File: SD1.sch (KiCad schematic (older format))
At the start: 43 parts, among them J103 JST ZH 1.5mm 1x5, J107 FPC PMS, Q101 BSS138, Q102 PDTC114EU,115, SW103 Multidirection_Switch, SW104 Multifunction_Switch, U101 TLV70233_SOT23-5, U102 ER-TFTM028-4, U104 CC2652P, U106 EKMC1691111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

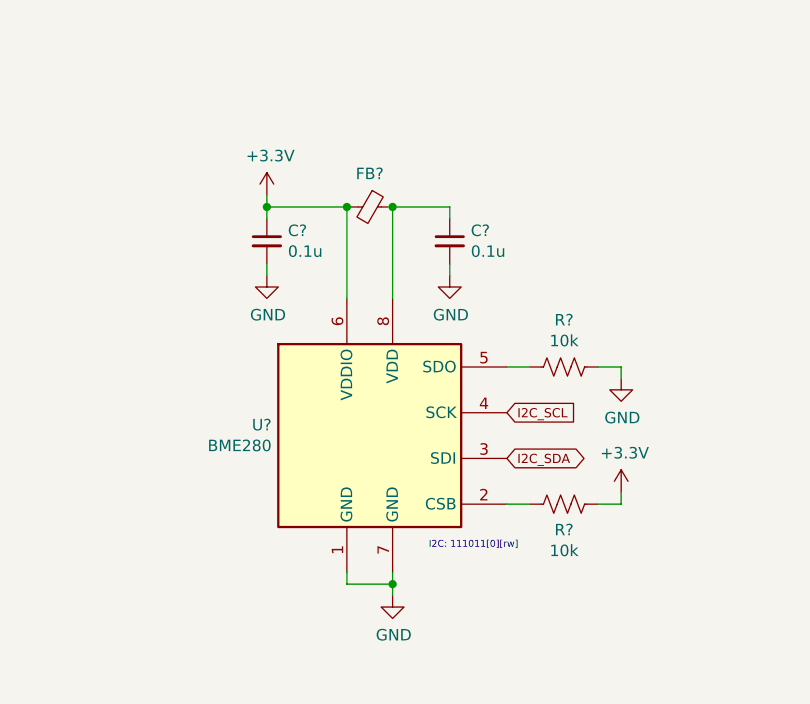
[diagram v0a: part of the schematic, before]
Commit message: Minor part picking and annotation
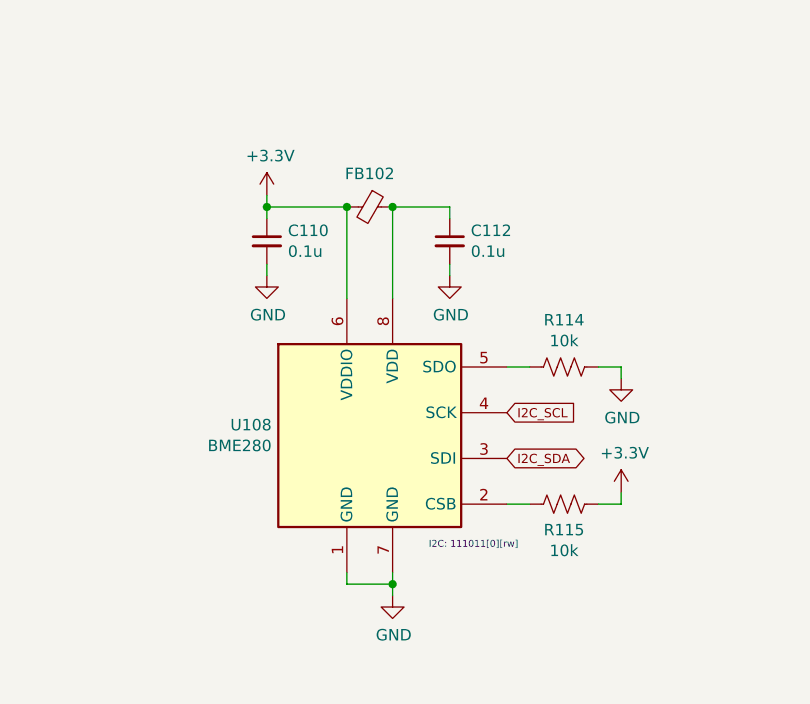
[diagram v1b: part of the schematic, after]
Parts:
- J103: Digikey (none) -> 455-1684-1-ND; LCSC (none) -> C265440; MPN (none) -> B5B-ZR-SM4-TF(LF)(SN)
- SW104: LCSC (none) -> C502286; MPN (none) -> K1-1508SA-03; Note (none) -> SMD Multi-Directional Switch Thumb
- U108: renamed from U?; LCSC C92489 -> C92489; Manufacturer (none) -> Bosch
- gave numbers to parts that had none: 5
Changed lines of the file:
@@
 F 2 "mylib:K1-1508SA-01" H 5200 9460 50  0001 C CNN
 F 3 "~" H 5350 9560 50  0001 C CNN
+F 4 "C502286" H 5350 9300 50  0001 C CNN "LCSC"
+F 5 "K1-1508SA-03" H 5350 9300 50  0001 C CNN "MPN"
+F 6 "SMD Multi-Directional Switch Thumb" H 5350 9300 50  0001 C CNN "Note"
 	1    5350 9300
 	1    0    0    -1
@@
 F 3 "~" H 6250 8100 50  0001 C CNN
 F 4 "1.5mm 01x05 JST ZH" H 6250 8100 50  0001 C CNN "Note"
+F 5 "B5B-ZR-SM4-TF(LF)(SN)" H 6250 8100 50  0001 C CNN "MPN"
+F 6 "455-1684-1-ND" H 6250 8100 50  0001 C CNN "Digikey"
+F 7 "C265440" H 6250 8100 50  0001 C CNN "LCSC"
 	1    6250 8100
 	1    0    0    1
@@
 SERCOM 0
 $Comp
-L power:GND #PWR?
+L power:GND #PWR0187
 U 1 1 5FB0CAA2
 P 12050 8800
-F 0 "#PWR?" H 12050 8550 50  0001 C CNN
+F 0 "#PWR0187" H 12050 8550 50  0001 C CNN
 F 1 "GND" H 12055 8627 50  0000 C CNN
 F 2 "" H 12050 8800 50  0001 C CNN
@@
 	11500 7150 11500 7100
 $Comp
-L power:+3.3V #PWR?
+L power:+3.3V #PWR0188
 U 1 1 5FB0CAA9
 P 11500 7050
-F 0 "#PWR?" H 11500 6900 50  0001 C CNN
+F 0 "#PWR0188" H 11500 6900 50  0001 C CNN
 F 1 "+3.3V" H 11515 7223 50  0000 C CNN
 F 2 "" H 11500 7050 50  0001 C CNN
@@
 $EndComp
 $Comp
-L Sensor:BME280 U?
+L Sensor:BME280 U108
 U 1 1 5FB0CAB4
 P 11950 8100
-F 0 "U?" H 11521 8146 50  0000 R CNN
+F 0 "U108" H 11521 8146 50  0000 R CNN
 F 1 "BME280" H 11521 8055 50  0000 R CNN
 F 2 "Package_LGA:Bosch_LGA-8_2.5x2.5mm_P0.65mm_ClockwisePinNumbering" H 13450 7650 50  0001 C CNN
@@
 F 6 "Humidity Temperature Sensor 0 ~ 100% RH I²C, SPI ±3% 1s Surface Mount" H 11950 8100 50  0001 C CNN "Note"
 F 7 "262-BME280" H 11950 8100 50  0001 C CNN "Mouser"
-F 8 " C92489 " H 11950 8100 50  0001 C CNN "LCSC"
+F 8 "C92489 " H 11950 8100 50  0001 C CNN "LCSC"
+F 9 "Bosch" H 11950 8100 50  0001 C CNN "Manufacturer"
 	1    11950 8100
 	1    0    0    -1
@@
 	12550 8400 12650 8400
 $Comp
-L power:+3.3V #PWR?
+L power:+3.3V #PWR0189
 U 1 1 5FB0CABB
 P 13050 8350
-F 0 "#PWR?" H 13050 8200 50  0001 C CNN
+F 0 "#PWR0189" H 13050 8200 50  0001 C CNN
 F 1 "+3.3V" H 13065 8523 50  0000 C CNN
 F 2 "" H 13050 8350 50  0001 C CNN
@@
 	13050 8400 13050 8350
 $Comp
-L Device:R_US R?
+L Device:R_US R114
 U 1 1 5FB0CAC7
 P 12800 7800
-F 0 "R?" V 13005 7800 50  0000 C CNN
+F 0 "R114" V 13005 7800 50  0000 C CNN
 F 1 "10k" V 12914 7800 50  0000 C CNN
 F 2 "Resistor_SMD:R_0603_1608Metric" H 12800 7800 60  0001 C CNN
@@
 $EndComp
 $Comp
-L Device:R_US R?
+L Device:R_US R115
 U 1 1 5FB0CAD0
 P 12800 8400
-F 0 "R?" V 12687 8400 50  0000 C CNN
+F 0 "R115" V 12687 8400 50  0000 C CNN
 F 1 "10k" V 12596 8400 50  0000 C CNN
 F 2 "Resistor_SMD:R_0603_1608Metric" H 12800 8400 60  0001 C CNN
@@
 $EndComp
 $Comp
-L Device:Ferrite_Bead_Small FB?
+L Device:Ferrite_Bead_Small FB102
 U 1 1 5FB0CADA
 P 11950 7100
-F 0 "FB?" V 11805 7100 50  0000 C CNN
+F 0 "FB102" V 11805 7100 50  0000 C CNN
 F 1 "Ferrite_Bead_Small" V 11804 7100 50  0001 C CNN
 F 2 "Inductor_SMD:L_0603_1608Metric" V 11880 7100 50  0001 C CNN
@@
 Connection ~ 11500 7100
 $Comp
-L power:GND #PWR?
+L power:GND #PWR0190
 U 1 1 5FB0CAE3
 P 12300 7400
-F 0 "#PWR?" H 12300 7150 50  0001 C CNN
+F 0 "#PWR0190" H 12300 7150 50  0001 C CNN
 F 1 "GND" H 12305 7227 50  0000 C CNN
 F 2 "" H 12300 7400 50  0001 C CNN
@@
 	12300 7350 12300 7400
 $Comp
-L power:GND #PWR?
+L power:GND #PWR0191
 U 1 1 5FB0CAED
 P 11500 7400
-F 0 "#PWR?" H 11500 7150 50  0001 C CNN
+F 0 "#PWR0191" H 11500 7150 50  0001 C CNN
 F 1 "GND" H 11505 7227 50  0000 C CNN
 F 2 "" H 11500 7400 50  0001 C CNN
@@
 P 11500 7250
 AR Path="/5E360A9B/5FB0CAFA" Ref="C?"  Part="1"
-AR Path="/5FB0CAFA" Ref="C?"  Part="1"
+AR Path="/5FB0CAFA" Ref="C110"  Part="1"
 AR Path="/5E49A000/5FB0CAFA" Ref="C?"  Part="1"
 AR Path="/5E5C8043/5E49A000/5FB0CAFA" Ref="C?"  Part="1"
 AR Path="/5E5C8043/5EAB3002/5FB0CAFA" Ref="C?"  Part="1"
 AR Path="/5E5C8043/5FB0CAFA" Ref="C?"  Part="1"
-F 0 "C?" H 11592 7296 50  0000 L CNN
+F 0 "C110" H 11592 7296 50  0000 L CNN
 F 1 "0.1u" H 11592 7205 50  0000 L CNN
 F 2 "Capacitor_SMD:C_0603_1608Metric" H 11500 7250 50  0001 C CNN
@@
 P 12300 7250
 AR Path="/5E360A9B/5FB0CB03" Ref="C?"  Part="1"
-AR Path="/5FB0CB03" Ref="C?"  Part="1"
+AR Path="/5FB0CB03" Ref="C112"  Part="1"
 AR Path="/5E49A000/5FB0CB03" Ref="C?"  Part="1"
 AR Path="/5E5C8043/5E49A000/5FB0CB03" Ref="C?"  Part="1"
 AR Path="/5E5C8043/5EAB3002/5FB0CB03" Ref="C?"  Part="1"
 AR Path="/5E5C8043/5FB0CB03" Ref="C?"  Part="1"
-F 0 "C?" H 12392 7296 50  0000 L CNN
+F 0 "C112" H 12392 7296 50  0000 L CNN
 F 1 "0.1u" H 12392 7205 50  0000 L CNN
 F 2 "Capacitor_SMD:C_0603_1608Metric" H 12300 7250 50  0001 C CNN
@@
 	12550 7800 12650 7800
 $Comp
-L power:GND #PWR?
+L power:GND #PWR0192
 U 1 1 5FB0CB0B
 P 13050 7850
-F 0 "#PWR?" H 13050 7600 50  0001 C CNN
+F 0 "#PWR0192" H 13050 7600 50  0001 C CNN
 F 1 "GND" H 13055 7677 50  0000 C CNN
 F 2 "" H 13050 7850 50  0001 C CNN

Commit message: Add SCD30 co2 sensor
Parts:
- added C114: 10u, Capacitor_SMD:C_0603_1608Metric, symbol Device:C_Small
- added U109: SCD30, mylib:SCD30, symbol mylib:SCD30
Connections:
- wire segments 189 -> 199
- no-connect marks 29 -> 31
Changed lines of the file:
@@
 Text Notes 12600 8600 2    30   ~ 0
 I2C: 111011[0][rw]
+Text Notes -35300 -1500 1    50   ~ 0
+SERCOM 0
+Text Notes -35300 -1500 1    50   ~ 0
+SERCOM 0
+Text Notes -35300 -1500 1    50   ~ 0
+SERCOM 0
+Text Notes -35300 -1500 1    50   ~ 0
+SERCOM 0
+Text Notes -35300 -1500 1    50   ~ 0
+SERCOM 0
+Text Notes -35300 -1500 1    50   ~ 0
+SERCOM 0
+Text Notes -35300 -1500 1    50   ~ 0
+SERCOM 0
+Text Notes -35300 -1500 1    50   ~ 0
+SERCOM 0
+Text Notes -35300 -1500 1    50   ~ 0
+SERCOM 0
+Connection ~ 14300 8400
+Wire Wire Line
+	14300 8300 14300 8400
+Wire Wire Line
+	14300 8500 14300 8400
+$Comp
+L power:GND #PWR0193
+U 1 1 5FAABC78
+P 14300 8500
+F 0 "#PWR0193" H 14300 8250 50  0001 C CNN
+F 1 "GND" H 14305 8327 50  0000 C CNN
+F 2 "" H 14300 8500 50  0001 C CNN
+F 3 "" H 14300 8500 50  0001 C CNN
+	1    14300 8500
+	1    0    0    -1
+$EndComp
+NoConn ~ 14400 8100
+NoConn ~ 14400 8200
+Wire Wire Line
+	14400 8400 14300 8400
+Wire Wire Line
+	14400 8300 14300 8300
+Wire Wire Line
+	14400 7750 14300 7750
+$Comp
+L mylib:SCD30 U109
+U 1 1 5FAABC3D
+P 14800 8050
+F 0 "U109" H 14497 8071 50  0000 R CNN
+F 1 "SCD30" H 14497 7980 50  0000 R CNN
+F 2 "mylib:SCD30" V 14800 8050 50  0001 C CNN
+F 3 "https://www.sensirion.com/fileadmin/user_upload/customers/sensirion/Dokumente/9.5_CO2/Sensirion_CO2_Sensors_SCD30_Datasheet.pdf" V 15075 8225 50  0001 C CNN
+F 4 "SCD30" H 14800 8050 50  0001 C CNN "MPN"
+F 5 "1649-1098-ND" H 14800 8050 50  0001 C CNN "Digikey"
+F 6 "CO2 SENSOR I2C/MODBUS/PWM DIGITL" H 14800 8050 50  0001 C CNN "Note"
+F 7 "Sensirion" H 14800 8050 50  0001 C CNN "Manufacturer"
+F 8 "403-SCD30" H 14800 8050 50  0001 C CNN "Mouser"
+	1    14800 8050
+	-1   0    0    -1
+$EndComp
+Text GLabel 14400 7900 0    40   BiDi ~ 0
+I2C_SDA
+Text GLabel 14400 8000 0    40   Input ~ 0
+I2C_SCL
+Wire Wire Line
+	14100 7350 14300 7350
+Wire Wire Line
+	14300 7300 14300 7350
+Connection ~ 14300 7350
+Wire Wire Line
+	14100 7400 14100 7350
+$Comp
+L power:GND #PWR0194
+U 1 1 5FBA1EBF
+P 14100 7650
+F 0 "#PWR0194" H 14100 7400 50  0001 C CNN
+F 1 "GND" H 14250 7600 50  0000 C CNN
+F 2 "" H 14100 7650 50  0001 C CNN
+F 3 "" H 14100 7650 50  0001 C CNN
+	1    14100 7650
+	-1   0    0    -1
+$EndComp
+Wire Wire Line
+	14100 7650 14100 7600
+$Comp
+L Device:C_Small C114
+U 1 1 5FBAEF7F
+P 14100 7500
+F 0 "C114" H 14192 7546 50  0000 L CNN
+F 1 "10u" H 14192 7455 50  0000 L CNN
+F 2 "Capacitor_SMD:C_0603_1608Metric" H 14100 7500 50  0001 C CNN
+F 3 "" H 14100 7500 50  0001 C CNN
+F 4 "445-6853-1-ND" H 14100 7500 50  0001 C CNN "Digikey"
+F 5 "C1608X5R1A106M080AC" H 14100 7500 50  0001 C CNN "MPN"
+F 6 "CAP CER 10UF 10V X5R 0603" H 14100 7500 50  0001 C CNN "Note"
+	1    14100 7500
+	-1   0    0    -1
+$EndComp
+Wire Wire Line
+	14300 7350 14300 7750
+$Comp
+L power:+5V #PWR0195
+U 1 1 5FBCBF4F
+P 14300 7300
+F 0 "#PWR0195" H 14300 7150 50  0001 C CNN
+F 1 "+5V" H 14315 7473 50  0000 C CNN
+F 2 "" H 14300 7300 50  0001 C CNN
+F 3 "" H 14300 7300 50  0001 C CNN
+	1    14300 7300
+	-1   0    0    -1
+$EndComp
 $EndSCHEMATC

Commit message: Major power changes
Added 5v boost, 3.3 buck, ideal diode circuits.
Poe: added barrel jacks
Smoke: general cleanup
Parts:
- removed C105, C106: 1u, Capacitor_SMD:C_0603_1608Metric, symbol Device:C_Small
- removed U101: TLV70233_SOT23-5, Package_TO_SOT_SMD:SOT-23-5, symbol Regulator_Linear:TLV70233_SOT23-5
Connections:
- net labels added: 5V_MainDet, EN_5V_BST
- net labels removed: SYS_PWR
- wire segments 199 -> 188
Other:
- note removed: "5.5V, 300mA max"
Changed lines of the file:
@@
 $Descr A3 16535 11693
 encoding utf-8
-Sheet 1 7
+Sheet 1 8
 Title ""
 Date ""
@@
 Text Notes -35300 -1500 1    50   ~ 0
 SERCOM 0
-$Comp
-L Device:C_Small C?
-U 1 1 5E6A4789
-P 2200 1100
-AR Path="/5E360A9B/5E6A4789" Ref="C?"  Part="1"
-AR Path="/5E6A4789" Ref="C106"  Part="1"
-AR Path="/5E5C8043/5E5C885F/5E6A4789" Ref="C?"  Part="1"
-AR Path="/5E5C8043/5E9EE9F0/5E6A4789" Ref="C?"  Part="1"
-AR Path="/5E5C8043/5EA19CBA/5E6A4789" Ref="C?"  Part="1"
-AR Path="/5E5C8043/5E49A000/5E6A4789" Ref="C?"  Part="1"
-AR Path="/5E5C8043/5EAB3002/5E6A4789" Ref="C?"  Part="1"
-AR Path="/5E5C8043/5E6A4789" Ref="C?"  Part="1"
-F 0 "C106" H 2108 1146 50  0000 R CNN
-F 1 "1u" H 2108 1055 50  0000 R CNN
-F 2 "Capacitor_SMD:C_0603_1608Metric" H 2200 1100 50  0001 C CNN
-F 3 "~" H 2200 1100 50  0001 C CNN
-F 4 "TMK107B7105KA-T" H 2200 1100 50  0001 C CNN "MPN"
-F 5 "587-2984-1-ND" H 2200 1100 50  0001 C CNN "Digikey"
-F 6 "CAP CER 1UF 25V X7R 0603" H 2200 1100 50  0001 C CNN "Note"
-	1    2200 1100
-	-1   0    0    -1
-$EndComp
 Text Notes -35300 -1500 1    50   ~ 0
 SERCOM 0
-Wire Wire Line
-	2100 950  2200 950
-$Comp
-L power:+3.3V #PWR?
-U 1 1 5E8C9DE5
-P 2450 950
-AR Path="/5E715318/5E8C9DE5" Ref="#PWR?"  Part="1"
-AR Path="/5E8C9DE5" Ref="#PWR0101"  Part="1"
-F 0 "#PWR0101" H 2450 800 50  0001 C CNN
-F 1 "+3.3V" H 2465 1123 50  0000 C CNN
-F 2 "" H 2450 950 50  0001 C CNN
-F 3 "" H 2450 950 50  0001 C CNN
-	1    2450 950
-	-1   0    0    -1
-$EndComp
-Wire Wire Line
-	2200 1000 2200 950
-Connection ~ 2200 950
-Wire Wire Line
-	2200 950  2450 950
-$Comp
-L power:GND #PWR?
-U 1 1 5E8C9DEE
-P 2200 1450
-AR Path="/5E715318/5E8C9DEE" Ref="#PWR?"  Part="1"
-AR Path="/5E8C9DEE" Ref="#PWR0109"  Part="1"
-F 0 "#PWR0109" H 2200 1200 50  0001 C CNN
-F 1 "GND" H 2205 1277 50  0000 C CNN
-F 2 "" H 2200 1450 50  0001 C CNN
-F 3 "" H 2200 1450 50  0001 C CNN
-	1    2200 1450
-	-1   0    0    -1
-$EndComp
-Wire Wire Line
-	2200 1200 2200 1450
-$Comp
-L power:GND #PWR?
-U 1 1 5E8C9DF5
-P 1800 1450
-AR Path="/5E715318/5E8C9DF5" Ref="#PWR?"  Part="1"
-AR Path="/5E8C9DF5" Ref="#PWR0108"  Part="1"
-F 0 "#PWR0108" H 1800 1200 50  0001 C CNN
-F 1 "GND" H 1805 1277 50  0000 C CNN
-F 2 "" H 1800 1450 50  0001 C CNN
-F 3 "" H 1800 1450 50  0001 C CNN
-	1    1800 1450
-	-1   0    0    -1
-$EndComp
-Wire Wire Line
-	1800 1450 1800 1350
-Wire Wire Line
-	1500 1050 1450 1050
-Wire Wire Line
-	1450 1050 1450 950
-Connection ~ 1450 950
-Wire Wire Line
-	1450 950  1500 950
-Text Notes 1850 1800 0    50   ~ 0
-5.5V, 300mA max
-$Comp
-L Regulator_Linear:TLV70233_SOT23-5 U?
-U 1 1 5E8C9E0D
-P 1800 1050
-AR Path="/5E715318/5E8C9E0D" Ref="U?"  Part="1"
-AR Path="/5E8C9E0D" Ref="U101"  Part="1"
-F 0 "U101" H 1800 1392 50  0000 C CNN
-F 1 "TLV70233_SOT23-5" H 1800 1301 50  0000 C CNN
-F 2 "Package_TO_SOT_SMD:SOT-23-5" H 1800 1375 50  0001 C CIN
-F 3 "http://www.ti.com/lit/ds/symlink/tlv702.pdf" H 1800 1100 50  0001 C CNN
-F 4 "TLV70233DBVR" H 1800 1050 50  0001 C CNN "MPN"
-F 5 "296-32415-1-ND " H 1800 1050 50  0001 C CNN "Digikey"
-F 6 "IC REG LINEAR 3.3V 300MA SOT23-5" H 1800 1050 50  0001 C CNN "Note"
-F 7 "C26833" H 1800 1050 50  0001 C CNN "LCSC"
-F 8 "Texas Instruments" H 1800 1050 50  0001 C CNN "Manufacturer"
-	1    1800 1050
-	1    0    0    -1
-$EndComp
-Wire Wire Line
-	950  950  1100 950
-Wire Wire Line
-	1100 1000 1100 950
-Connection ~ 1100 950
-Wire Wire Line
-	1100 950  1450 950
-$Comp
-L power:GND #PWR?
-U 1 1 5E8C9E17
-P 1100 1450
-AR Path="/5E715318/5E8C9E17" Ref="#PWR?"  Part="1"
-AR Path="/5E8C9E17" Ref="#PWR0107"  Part="1"
-F 0 "#PWR0107" H 1100 1200 50  0001 C CNN
-F 1 "GND" H 1105 1277 50  0000 C CNN
-F 2 "" H 1100 1450 50  0001 C CNN
-F 3 "" H 1100 1450 50  0001 C CNN
-	1    1100 1450
-	-1   0    0    -1
-$EndComp
-Wire Wire Line
-	1100 1200 1100 1450
-$Comp
-L Device:C_Small C?
-U 1 1 5E90B519
-P 1100 1100
-AR Path="/5E360A9B/5E90B519" Ref="C?"  Part="1"
-AR Path="/5E90B519" Ref="C105"  Part="1"
-AR Path="/5E5C8043/5E5C885F/5E90B519" Ref="C?"  Part="1"
-AR Path="/5E5C8043/5E9EE9F0/5E90B519" Ref="C?"  Part="1"
-AR Path="/5E5C8043/5EA19CBA/5E90B519" Ref="C?"  Part="1"
-AR Path="/5E5C8043/5E49A000/5E90B519" Ref="C?"  Part="1"
-AR Path="/5E5C8043/5EAB3002/5E90B519" Ref="C?"  Part="1"
-AR Path="/5E5C8043/5E90B519" Ref="C?"  Part="1"
-F 0 "C105" H 1008 1146 50  0000 R CNN
-F 1 "1u" H 1008 1055 50  0000 R CNN
-F 2 "Capacitor_SMD:C_0603_1608Metric" H 1100 1100 50  0001 C CNN
-F 3 "~" H 1100 1100 50  0001 C CNN
-F 4 "TMK107B7105KA-T" H 1100 1100 50  0001 C CNN "MPN"
-F 5 "587-2984-1-ND" H 1100 1100 50  0001 C CNN "Digikey"
-F 6 "CAP CER 1UF 25V X7R 0603" H 1100 1100 50  0001 C CNN "Note"
-	1    1100 1100
-	-1   0    0    -1
-$EndComp
 Text Notes 14550 11650 0    60   ~ 0
 Barrel Jack:\n5.5mm OD\n2.1mm ID/Pole
@@
 EndData
 $EndBitmap
-Text GLabel 950  950  0    50   Input ~ 0
-SYS_PWR
 $Comp
 L Transistor_FET:BSS138 Q101
@@
 	-1   0    0    -1
 $EndComp
+$Sheet
+S 3100 4750 900  600
+U 5FAF778C
+F0 "Power" 50
+F1 "power.sch" 50
+$EndSheet
+Text GLabel 4950 3450 0    50   Input ~ 0
+5V_MainDet
+Wire Wire Line
+	4500 3600 4950 3600
+Text Label 4500 3600 0    50   ~ 0
+EN_5V_BST
 $EndSCHEMATC

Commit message: Starting pin assignment
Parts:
- removed SW104: Multifunction_Switch, mylib:K1-1508SA-01, symbol mylib:Multifunction_Switch
- added R? (x2): 10k, Resistor_SMD:R_0603_1608Metric, symbol Device:R_US
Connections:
- net labels added: EXT_Sleep, Multi_A, Multi_B, Multi_C, Multi_D, Multi_Press
- net labels removed: TH_CLICK, TH_DOWN, TH_UP, ~BMS_INT, ~MPPT_EN
- wire segments 188 -> 209
- no-connect marks 31 -> 32
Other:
- note added: "Carbon Dioxide Sensor"
- note added: "Carbon Monoxide Sensor"
- note added: "External / Additional Sensor Connector"
- note added: "Motion Detection"
- note added: "Particulates"
- note added: "Smoke Sensor"
- note added: "Temp / Humidity / Pressure"
- note added: "Volatile Organic Compounds"
- moved on the sheet: $U101, C109, C110, C112, C114, C115, D105, FB102, J103, J107, LS101, Q101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

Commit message: Continue part picking
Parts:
- FB102: LCSC (none) -> C97853
- U107: Digikey MCP23017T-E/SOCT-ND -> MCP23017T-E/SSCT-ND; MPN MCP23017T-E/SO -> MCP23017T-E/SS; Mouser - -> (none); Note (none) -> IC I/O EXPANDER 16BIT I2C 28SSOP
- gave numbers to parts that had none: 2
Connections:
- net +3V3: now also LS101.1, R108.2
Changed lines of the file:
@@
 F 2 "Package_SO:SSOP-28_5.3x10.2mm_P0.65mm" H 10000 1600 50  0001 L CNN
 F 3 "" H 10200 3550 50  0001 C CNN
-F 4 "MCP23017T-E/SO" H 9950 2550 60  0001 C CNN "MPN"
-F 5 "-" H 9950 2550 60  0001 C CNN "Mouser"
-F 6 "MCP23017T-E/SOCT-ND" H 9950 2550 60  0001 C CNN "Digikey"
+F 4 "MCP23017T-E/SS" H 9950 2550 60  0001 C CNN "MPN"
+F 5 "" H 9950 2550 60  0001 C CNN "Mouser"
+F 6 "MCP23017T-E/SSCT-ND" H 9950 2550 60  0001 C CNN "Digikey"
+F 7 "IC I/O EXPANDER 16BIT I2C 28SSOP" H 9950 2550 50  0001 C CNN "Note"
 	1    9950 2550
 	1    0    0    -1
@@
 F 6 "490-5223-1-ND" H 8300 6750 50  0001 C CNN "Digikey"
 F 7 "470 Ohms @ 100MHz 1 Power Line Ferrite Bead 0603 1A 200mOhm" H 8300 6750 50  0001 C CNN "Note"
+F 8 "C97853" H 8300 6750 50  0001 C CNN "LCSC"
 	1    8300 6750
 	0    1    1    0
@@
 Multi_D
 $Comp
-L power:GND #PWR?
+L power:GND #PWR0101
 U 1 1 6056C8D2
 P 15700 3400
-F 0 "#PWR?" H 15700 3150 50  0001 C CNN
+F 0 "#PWR0101" H 15700 3150 50  0001 C CNN
 F 1 "GND" H 15705 3227 50  0000 C CNN
 F 2 "" H 15700 3400 50  0001 C CNN
@@
 	11150 1950 10650 1950
 $Comp
-L Device:R_US R?
+L Device:R_US R116
 U 1 1 607EAA0B
 P 1150 4050
-F 0 "R?" H 1218 4096 50  0000 L CNN
+F 0 "R116" H 1218 4096 50  0000 L CNN
 F 1 "10k" H 1218 4005 50  0000 L CNN
 F 2 "Resistor_SMD:R_0603_1608Metric" H 1150 4050 60  0001 C CNN
@@
 $EndComp
 $Comp
-L Device:R_US R?
+L Device:R_US R117
 U 1 1 607EB21C
 P 1550 4050
-F 0 "R?" H 1618 4096 50  0000 L CNN
+F 0 "R117" H 1618 4096 50  0000 L CNN
 F 1 "10k" H 1618 4005 50  0000 L CNN
 F 2 "Resistor_SMD:R_0603_1608Metric" H 1550 4050 60  0001 C CNN
@@
 P 1150 3650
 AR Path="/5E715318/608222AB" Ref="#PWR?"  Part="1"
-AR Path="/608222AB" Ref="#PWR?"  Part="1"
-F 0 "#PWR?" H 1150 3500 50  0001 C CNN
+AR Path="/608222AB" Ref="#PWR0107"  Part="1"
+F 0 "#PWR0107" H 1150 3500 50  0001 C CNN
 F 1 "+3.3V" H 1165 3823 50  0000 C CNN
 F 2 "" H 1150 3650 50  0001 C CNN
@@
 P 1550 3650
 AR Path="/5E715318/60822983" Ref="#PWR?"  Part="1"
-AR Path="/60822983" Ref="#PWR?"  Part="1"
-F 0 "#PWR?" H 1550 3500 50  0001 C CNN
+AR Path="/60822983" Ref="#PWR0108"  Part="1"
+F 0 "#PWR0108" H 1550 3500 50  0001 C CNN
 F 1 "+3.3V" H 1565 3823 50  0000 C CNN
 F 2 "" H 1550 3650 50  0001 C CNN
@@
 	-1   0    0    -1
 $EndComp
+Wire Wire Line
+	12750 8200 12750 8100
+$Comp
+L power:+3.3V #PWR?
+U 1 1 6092EB6F
+P 12750 8100
+AR Path="/5E715318/6092EB6F" Ref="#PWR?"  Part="1"
+AR Path="/6092EB6F" Ref="#PWR?"  Part="1"
+F 0 "#PWR?" H 12750 7950 50  0001 C CNN
+F 1 "+3.3V" H 12765 8273 50  0000 C CNN
+F 2 "" H 12750 8100 50  0001 C CNN
+F 3 "" H 12750 8100 50  0001 C CNN
+	1    12750 8100
+	-1   0    0    -1
+$EndComp
+Connection ~ 12750 8200
 $EndSCHEMATC
